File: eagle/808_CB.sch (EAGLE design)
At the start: 54 parts, among them IC1 4584N, IC2 TL072P, Q1 2N3904, Q2 2N3904, Q3 2N3904, Q4 2N3906, X1 22-23-2021

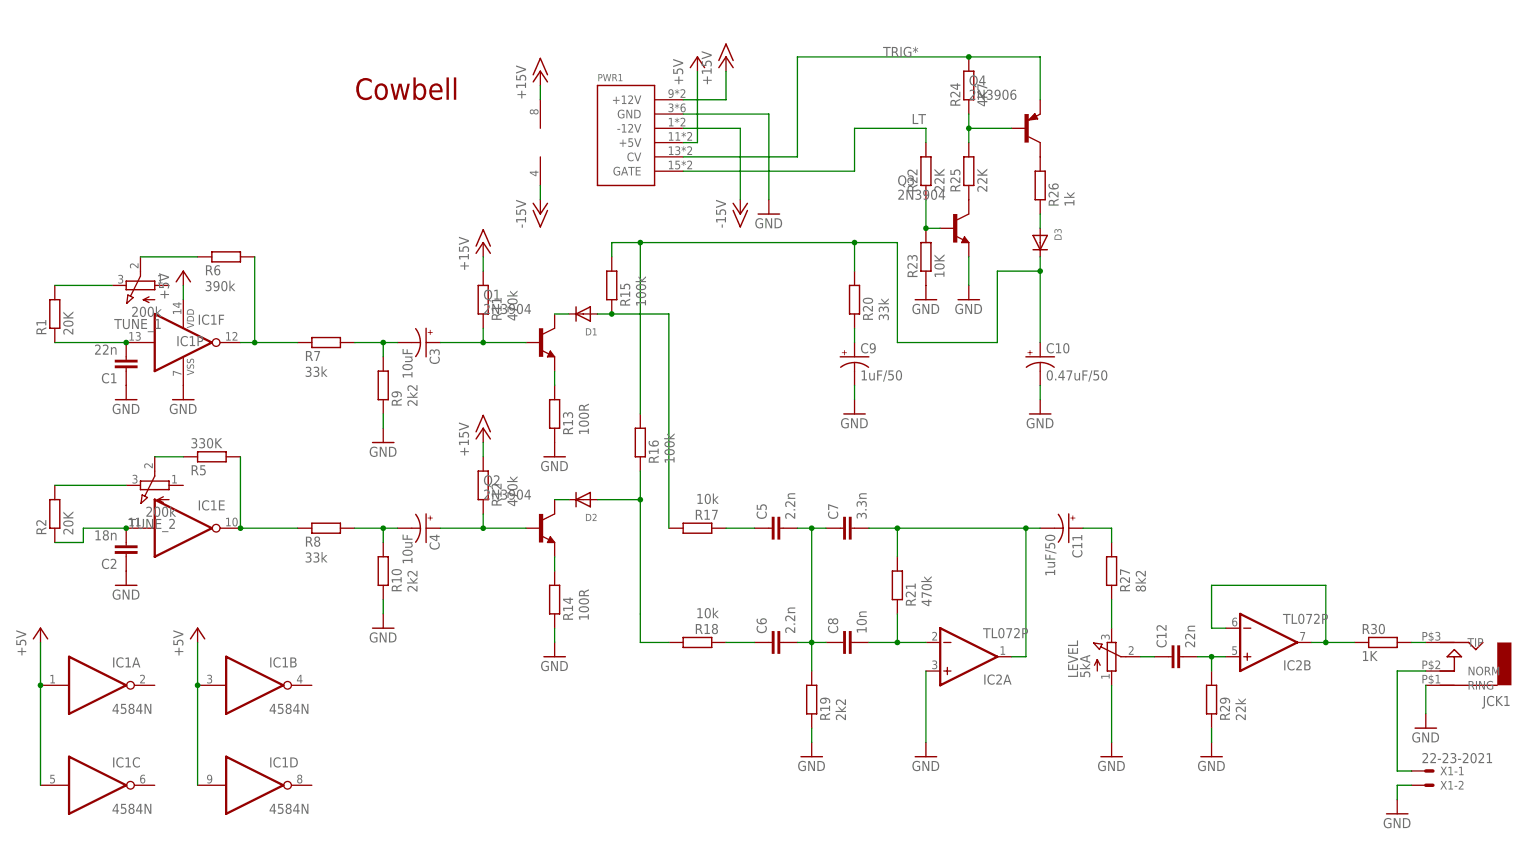
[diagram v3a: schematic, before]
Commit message: trigger and accent pads
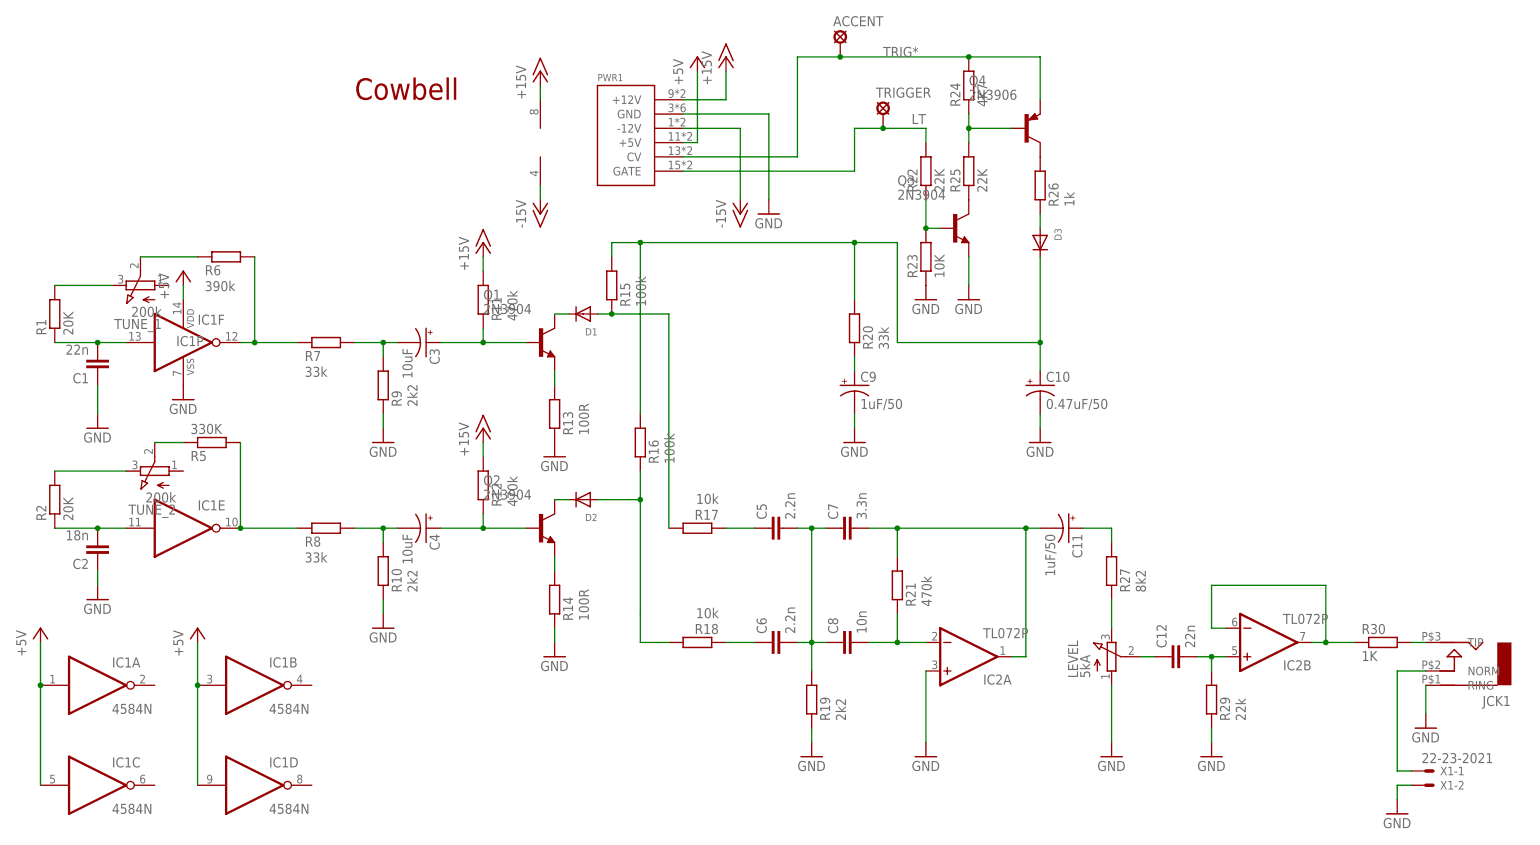
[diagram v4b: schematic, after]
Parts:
- added ACCENT, TRIGGER: LSP11, solpad:LSP11
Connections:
- net LT: now also TRIGGER.MP
- net TRIG*: now also ACCENT.MP
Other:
- moved on the sheet: C1, C10, C2, C9, R2, R20, R5, TUNE_2
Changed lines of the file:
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@@
 <part name="GND17" library="supply1" deviceset="GND" device=""/>
 <part name="GND16" library="supply1" deviceset="GND" device=""/>
+<part name="TRIGGER" library="solpad" deviceset="LSP11" device=""/>
+<part name="ACCENT" library="solpad" deviceset="LSP11" device=""/>
 </parts>
 <sheets>
@@
 </plain>
 <instances>
-<instance part="GND14" gate="1" x="127" y="27.94"/>
+<instance part="GND14" gate="1" x="127" y="22.86"/>
 <instance part="R24" gate="G$1" x="114.3" y="86.36" rot="R90"/>
 <instance part="R25" gate="G$1" x="114.3" y="71.12" rot="R90"/>
@@
 <attribute name="NAME" x="-26.67" y="40.005" size="1.778" layer="95"/>
 </instance>
-<instance part="R5" gate="G$1" x="-20.32" y="20.32" rot="MR180"/>
-<instance part="C2" gate="G$1" x="-35.56" y="2.54" rot="R180"/>
-<instance part="C1" gate="G$1" x="-35.56" y="35.56" rot="R180"/>
-<instance part="GND2" gate="1" x="-35.56" y="-2.54"/>
-<instance part="GND1" gate="1" x="-35.56" y="30.48"/>
+<instance part="R5" gate="G$1" x="-20.32" y="22.86" rot="MR180"/>
+<instance part="C2" gate="G$1" x="-40.64" y="2.54" rot="R180"/>
+<instance part="C1" gate="G$1" x="-40.64" y="35.56" rot="R180"/>
+<instance part="GND2" gate="1" x="-40.64" y="-5.08"/>
+<instance part="GND1" gate="1" x="-40.64" y="25.4"/>
 <instance part="R6" gate="G$1" x="-17.78" y="55.88" smashed="yes" rot="MR180">
 <attribute name="NAME" x="-21.59" y="54.3814" size="1.778" layer="95" rot="MR180"/>
@@
 <instance part="P+2" gate="1" x="-25.4" y="53.34"/>
 <instance part="TUNE_1" gate="G$1" x="-33.02" y="50.8" rot="R90"/>
-<instance part="TUNE_2" gate="G$1" x="-30.48" y="15.24" rot="R90"/>
+<instance part="TUNE_2" gate="G$1" x="-30.48" y="17.78" rot="R90"/>
 <instance part="R1" gate="G$1" x="-48.26" y="45.72" rot="R90"/>
-<instance part="R2" gate="G$1" x="-48.26" y="10.16" rot="R90"/>
+<instance part="R2" gate="G$1" x="-48.26" y="12.7" rot="R90"/>
 <instance part="IC1" gate="A" x="-40.64" y="-20.32"/>
 <instance part="IC1" gate="B" x="-12.7" y="-20.32"/>
@@
 <instance part="D2" gate="G$1" x="45.72" y="12.7" rot="R180"/>
 <instance part="D1" gate="G$1" x="45.72" y="45.72" rot="R180"/>
-<instance part="C10" gate="G$1" x="127" y="38.1"/>
+<instance part="C10" gate="G$1" x="127" y="33.02"/>
 <instance part="R26" gate="G$1" x="127" y="68.58" smashed="yes" rot="MR90">
 <attribute name="NAME" x="128.4986" y="64.77" size="1.778" layer="95" rot="MR90"/>
@@
 </instance>
 <instance part="D3" gate="G$1" x="127" y="58.42" rot="R270"/>
-<instance part="R20" gate="G$1" x="93.98" y="48.26" smashed="yes" rot="MR90">
-<attribute name="NAME" x="95.4786" y="44.45" size="1.778" layer="95" rot="MR90"/>
-<attribute name="VALUE" x="98.298" y="44.45" size="1.778" layer="96" rot="MR90"/>
-</instance>
-<instance part="C9" gate="G$1" x="93.98" y="38.1"/>
-<instance part="GND10" gate="1" x="93.98" y="27.94"/>
+<instance part="R20" gate="G$1" x="93.98" y="43.18" smashed="yes" rot="MR90">
+<attribute name="NAME" x="95.4786" y="39.37" size="1.778" layer="95" rot="MR90"/>
+<attribute name="VALUE" x="98.298" y="39.37" size="1.778" layer="96" rot="MR90"/>
+</instance>
+<instance part="C9" gate="G$1" x="93.98" y="33.02"/>
+<instance part="GND10" gate="1" x="93.98" y="22.86"/>
 <instance part="R15" gate="G$1" x="50.8" y="50.8" smashed="yes" rot="MR90">
 <attribute name="NAME" x="52.2986" y="46.99" size="1.778" layer="95" rot="MR90"/>
@@
 <instance part="GND17" gate="1" x="190.5" y="-43.18"/>
 <instance part="GND16" gate="1" x="157.48" y="-33.02"/>
+<instance part="TRIGGER" gate="1" x="99.06" y="81.28"/>
+<instance part="ACCENT" gate="1" x="91.44" y="93.98"/>
 </instances>
 <busses>
@@
 <segment>
 <pinref part="GND14" gate="1" pin="GND"/>
-<wire x1="127" y1="30.48" x2="127" y2="33.02" width="0.1524" layer="91"/>
+<wire x1="127" y1="25.4" x2="127" y2="27.94" width="0.1524" layer="91"/>
 <pinref part="C10" gate="G$1" pin="-"/>
 </segment>
@@
 <pinref part="C2" gate="G$1" pin="1"/>
 <pinref part="GND2" gate="1" pin="GND"/>
+<wire x1="-40.64" y1="0" x2="-40.64" y2="-2.54" width="0.1524" layer="91"/>
 </segment>
 <segment>
 <pinref part="C1" gate="G$1" pin="1"/>
 <pinref part="GND1" gate="1" pin="GND"/>
+<wire x1="-40.64" y1="27.94" x2="-40.64" y2="33.02" width="0.1524" layer="91"/>
 </segment>
 <segment>
@@
 <pinref part="C9" gate="G$1" pin="-"/>
 <pinref part="GND10" gate="1" pin="GND"/>
-<wire x1="93.98" y1="33.02" x2="93.98" y2="30.48" width="0.1524" layer="91"/>
+<wire x1="93.98" y1="27.94" x2="93.98" y2="25.4" width="0.1524" layer="91"/>
 </segment>
 <segment>
@@
 <label x="99.06" y="91.44" size="1.778" layer="95"/>
 <junction x="114.3" y="91.44"/>
-<wire x1="114.3" y1="91.44" x2="83.82" y2="91.44" width="0.1524" layer="91"/>
+<wire x1="114.3" y1="91.44" x2="91.44" y2="91.44" width="0.1524" layer="91"/>
+<wire x1="91.44" y1="91.44" x2="83.82" y2="91.44" width="0.1524" layer="91"/>
 <wire x1="83.82" y1="91.44" x2="83.82" y2="73.66" width="0.1524" layer="91"/>
 <pinref part="PWR1" gate="G$1" pin="CV"/>
 <wire x1="83.82" y1="73.66" x2="63.5" y2="73.66" width="0.1524" layer="91"/>
 <pinref part="Q4" gate="G$1" pin="E"/>
+<pinref part="ACCENT" gate="1" pin="MP"/>
+<junction x="91.44" y="91.44"/>
 </segment>
 </net>
@@
 <wire x1="106.68" y1="76.2" x2="106.68" y2="78.74" width="0.1524" layer="91"/>
 <label x="106.68" y="81.28" size="1.778" layer="95" rot="R180"/>
-<wire x1="93.98" y1="78.74" x2="106.68" y2="78.74" width="0.1524" layer="91"/>
+<wire x1="93.98" y1="78.74" x2="99.06" y2="78.74" width="0.1524" layer="91"/>
+<pinref part="TRIGGER" gate="1" pin="MP"/>
+<wire x1="99.06" y1="78.74" x2="106.68" y2="78.74" width="0.1524" layer="91"/>
+<junction x="99.06" y="78.74"/>
 </segment>
 </net>
@@
 <pinref part="IC1" gate="E" pin="O"/>
 <pinref part="R5" gate="G$1" pin="2"/>
-<wire x1="-15.24" y1="20.32" x2="-15.24" y2="7.62" width="0.1524" layer="91"/>
+<wire x1="-15.24" y1="22.86" x2="-15.24" y2="7.62" width="0.1524" layer="91"/>
 <junction x="-15.24" y="7.62"/>
 <wire x1="-15.24" y1="7.62" x2="-5.08" y2="7.62" width="0.1524" layer="91"/>
@@
 <pinref part="IC1" gate="E" pin="I"/>
 <pinref part="C2" gate="G$1" pin="2"/>
-<wire x1="-35.56" y1="7.62" x2="-43.18" y2="7.62" width="0.1524" layer="91"/>
-<wire x1="-43.18" y1="7.62" x2="-43.18" y2="5.08" width="0.1524" layer="91"/>
-<junction x="-35.56" y="7.62"/>
+<wire x1="-40.64" y1="7.62" x2="-48.26" y2="7.62" width="0.1524" layer="91"/>
+<junction x="-40.64" y="7.62"/>
 <pinref part="R2" gate="G$1" pin="1"/>
-<wire x1="-43.18" y1="5.08" x2="-48.26" y2="5.08" width="0.1524" layer="91"/>
+<wire x1="-40.64" y1="7.62" x2="-35.56" y2="7.62" width="0.1524" layer="91"/>
 </segment>
 </net>
@@
 <pinref part="IC1" gate="F" pin="I"/>
 <pinref part="C1" gate="G$1" pin="2"/>
-<junction x="-35.56" y="40.64"/>
+<junction x="-40.64" y="40.64"/>
 <pinref part="R1" gate="G$1" pin="1"/>
-<wire x1="-35.56" y1="40.64" x2="-48.26" y2="40.64" width="0.1524" layer="91"/>
+<wire x1="-40.64" y1="40.64" x2="-48.26" y2="40.64" width="0.1524" layer="91"/>
+<wire x1="-40.64" y1="40.64" x2="-35.56" y2="40.64" width="0.1524" layer="91"/>
 </segment>
 </net>
@@
 <segment>
 <pinref part="R5" gate="G$1" pin="1"/>
-<wire x1="-30.48" y1="20.32" x2="-25.4" y2="20.32" width="0.1524" layer="91"/>
+<wire x1="-30.48" y1="22.86" x2="-25.4" y2="22.86" width="0.1524" layer="91"/>
 <pinref part="TUNE_2" gate="G$1" pin="S"/>
 </segment>
@@
 <pinref part="R2" gate="G$1" pin="2"/>
 <pinref part="TUNE_2" gate="G$1" pin="E"/>
-<wire x1="-48.26" y1="15.24" x2="-35.56" y2="15.24" width="0.1524" layer="91"/>
+<wire x1="-48.26" y1="17.78" x2="-35.56" y2="17.78" width="0.1524" layer="91"/>
 </segment>
 </net>
@@
 <pinref part="C10" gate="G$1" pin="+"/>
 <pinref part="D3" gate="G$1" pin="C"/>
-<wire x1="127" y1="55.88" x2="127" y2="53.34" width="0.1524" layer="91"/>
-<wire x1="127" y1="53.34" x2="127" y2="40.64" width="0.1524" layer="91"/>
-<wire x1="127" y1="53.34" x2="119.38" y2="53.34" width="0.1524" layer="91"/>
-<wire x1="119.38" y1="53.34" x2="119.38" y2="40.64" width="0.1524" layer="91"/>
-<junction x="127" y="53.34"/>
-<wire x1="119.38" y1="40.64" x2="101.6" y2="40.64" width="0.1524" layer="91"/>
+<wire x1="127" y1="55.88" x2="127" y2="40.64" width="0.1524" layer="91"/>
+<wire x1="127" y1="40.64" x2="127" y2="35.56" width="0.1524" layer="91"/>
+<junction x="127" y="40.64"/>
+<wire x1="127" y1="40.64" x2="101.6" y2="40.64" width="0.1524" layer="91"/>
 <wire x1="101.6" y1="40.64" x2="101.6" y2="58.42" width="0.1524" layer="91"/>
 <wire x1="101.6" y1="58.42" x2="93.98" y2="58.42" width="0.1524" layer="91"/>
 <pinref part="R20" gate="G$1" pin="2"/>
 <wire x1="93.98" y1="58.42" x2="55.88" y2="58.42" width="0.1524" layer="91"/>
-<wire x1="93.98" y1="53.34" x2="93.98" y2="58.42" width="0.1524" layer="91"/>
+<wire x1="93.98" y1="48.26" x2="93.98" y2="58.42" width="0.1524" layer="91"/>
 <junction x="93.98" y="58.42"/>
 <pinref part="R16" gate="G$1" pin="2"/>
@@
 <pinref part="R20" gate="G$1" pin="1"/>
 <pinref part="C9" gate="G$1" pin="+"/>
-<wire x1="93.98" y1="43.18" x2="93.98" y2="40.64" width="0.1524" layer="91"/>
-</segment>
-</net>
+<wire x1="93.98" y1="38.1" x2="93.98" y2="35.56" width="0.1524" layer="91"/>
+</segment>
+</net>

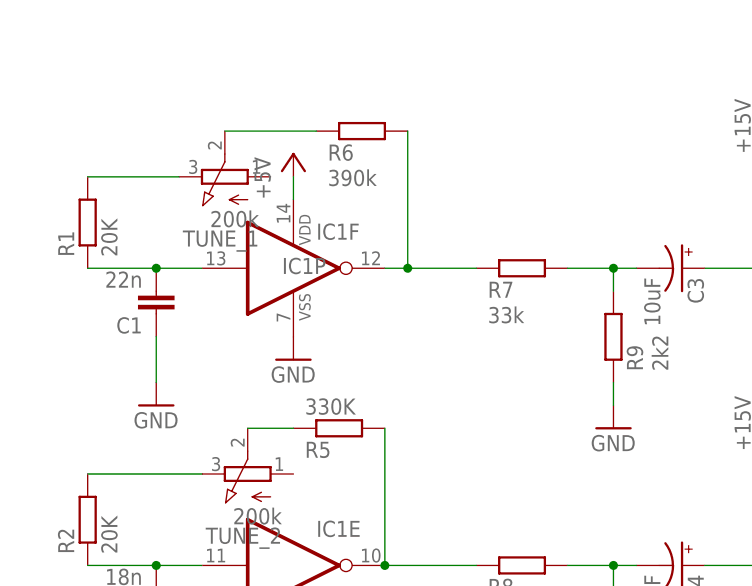
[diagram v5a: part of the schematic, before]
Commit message: switch back oscillator caps
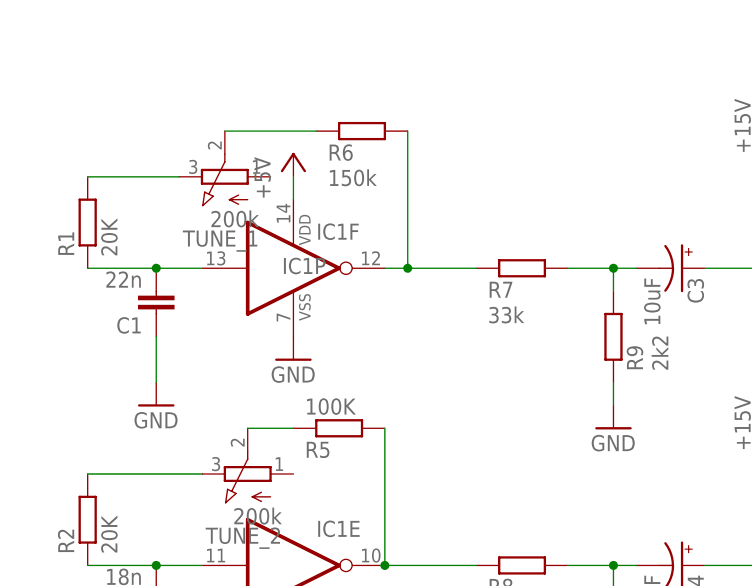
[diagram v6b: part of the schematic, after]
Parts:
- R5: value 330K -> 100K
- R6: value 390k -> 150k
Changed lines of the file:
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@@
 <?xml version="1.0" encoding="utf-8"?>
 <!DOCTYPE eagle SYSTEM "eagle.dtd">
-<eagle version="7.2.0">
+<eagle version="7.1.0">
 <drawing>
 <settings>
@@
 <part name="P-1" library="supply1" deviceset="-15V" device=""/>
 <part name="IC1" library="TR808clone" deviceset="4584" device="N"/>
-<part name="R5" library="TR808clone" deviceset="R-EU_" device="0207/5V" value="330K"/>
+<part name="R5" library="TR808clone" deviceset="R-EU_" device="0207/5V" value="100K"/>
 <part name="C2" library="TR808clone" deviceset="C-EU" device="4MM_PITCH" value="18n"/>
 <part name="C1" library="TR808clone" deviceset="C-EU" device="4MM_PITCH" value="22n"/>
 <part name="GND2" library="supply1" deviceset="GND" device=""/>
 <part name="GND1" library="supply1" deviceset="GND" device=""/>
-<part name="R6" library="TR808clone" deviceset="R-EU_" device="0207/5V" value="390k"/>
+<part name="R6" library="TR808clone" deviceset="R-EU_" device="0207/5V" value="150k"/>
 <part name="GND3" library="supply1" deviceset="GND" device=""/>
 <part name="P+2" library="supply1" deviceset="+5V" device=""/>
